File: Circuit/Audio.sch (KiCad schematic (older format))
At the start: 0 parts

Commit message: NAU8814 schematic component. LXDC2XQ footprint update. Kludge for forward/back slash in lib table needs addressing.
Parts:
- added U?: NAU8814, symbol NAU8814
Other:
- note added: "Mic Output - TRS jack?"
- note added: "Unused Analogue - Float\nUnused Digital - GND"
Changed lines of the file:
@@
 LIBS:lxdc2xq
 LIBS:qdtech-3.2-tft
+LIBS:nau8814
 LIBS:IoTuz-cache
 EELAYER 25 0
@@
 $Descr A4 11693 8268
 encoding utf-8
-Sheet 1 7
+Sheet 5 7
 Title ""
 Date ""
@@
 Comment4 ""
 $EndDescr
+$Comp
+L NAU8814 U?
+U 1 1 58192F60
+P 5600 3750
+F 0 "U?" H 5000 4450 60  0000 C CNN
+F 1 "NAU8814" H 6150 3050 60  0000 C CNN
+F 2 "" H 5600 3750 60  0001 C CNN
+F 3 "" H 5600 3750 60  0001 C CNN
+	1    5600 3750
+	1    0    0    -1
+$EndComp
+Text Notes 6300 4300 0    60   ~ 0
+Unused Analogue - Float\nUnused Digital - GND
+Text Notes 4350 2850 0    60   ~ 0
+Mic Output - TRS jack?
 $EndSCHEMATC

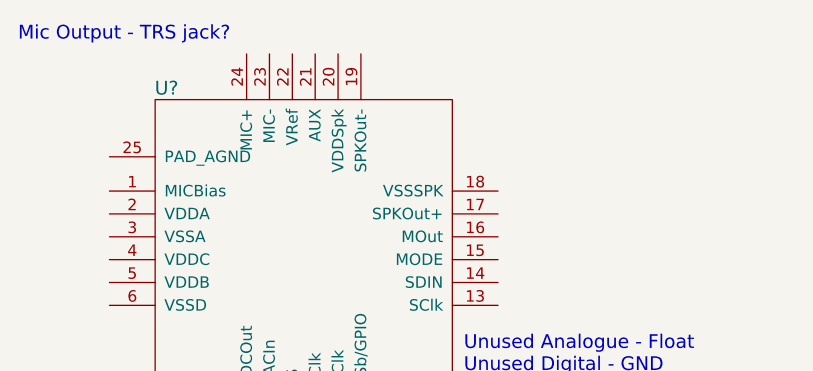
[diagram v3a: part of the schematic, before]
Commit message: Audio choices being narrowed.
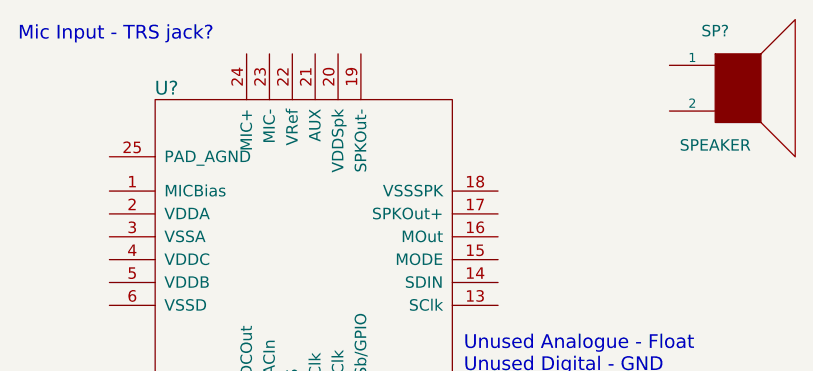
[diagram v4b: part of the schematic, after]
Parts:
- added SP?: SPEAKER, symbol SPEAKER
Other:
- note added: "Mic Input - TRS jack?"
- note removed: "Mic Output - TRS jack?"
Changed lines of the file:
@@
 Unused Analogue - Float\nUnused Digital - GND
 Text Notes 4350 2850 0    60   ~ 0
-Mic Output - TRS jack?
+Mic Input - TRS jack?
+$Comp
+L SPEAKER SP?
+U 1 1 581967C2
+P 7500 3050
+F 0 "SP?" H 7400 3300 50  0000 C CNN
+F 1 "SPEAKER" H 7400 2800 50  0000 C CNN
+F 2 "" H 7500 3050 50  0000 C CNN
+F 3 "" H 7500 3050 50  0000 C CNN
+F 4 "http://www.digikey.com.au/product-detail/en/cui-inc/CDM-12008/102-2494-ND/2791824" H 7500 3050 60  0001 C CNN "Link"
+F 5 "2.44000" H 7500 3050 60  0001 C CNN "Unit Cost"
+F 6 "102-2494-ND" H 7500 3050 60  0001 C CNN "Digikey PN"
+F 7 "CDM-12008" H 7500 3050 60  0001 C CNN "Manufacturer PN"
+	1    7500 3050
+	1    0    0    -1
+$EndComp
 $EndSCHEMATC

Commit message: Audio work, more to do.
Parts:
- added C?: 2.2uF, symbol C_Small
- added C? (x4): 4.7uF, symbol C
- added MK?: SPU0410HR5H, symbol SPU0410HR5H
- added R?: R, symbol R
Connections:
- net MICBias: now reaches U?.1 (MICBias)
- net MICBias: now also R?.1
- net AGND: now reaches U?.18 (VSSSPK)
- net AGND: now also U?.25 (PAD_AGND), U?.3 (VSSA), MK?.2 (GND), MK?.3 (GND)
- net +3V3: now reaches U?.20 (VDDSpk)
- net at U?.23 (MIC-): now also C?.2
- new net: MK?.1 (VIn), R?.2
- new net MICOut: C?.1, MK?.4 (Out)
- no-connect marks 0 -> 1
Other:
- note added: ""When the MIC- is used as a single ended input, \nMIC+ should be conned to VREF by setting PMICPGA[0] \naddress (0x2C) bit to LOW.""
- note added: "R needed?"
- note removed: "Mic Input - TRS jack?"
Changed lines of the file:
@@
 LIBS:qdtech-3.2-tft
 LIBS:nau8814
+LIBS:spu0410hr5h
 LIBS:IoTuz-cache
 EELAYER 25 0
@@
 Text Notes 6300 4300 0    60   ~ 0
 Unused Analogue - Float\nUnused Digital - GND
-Text Notes 4350 2850 0    60   ~ 0
-Mic Input - TRS jack?
 $Comp
 L SPEAKER SP?
@@
 	1    0    0    -1
 $EndComp
+Text Notes 600  900  0    60   ~ 0
+"When the MIC- is used as a single ended input, \nMIC+ should be conned to VREF by setting PMICPGA[0] \naddress (0x2C) bit to LOW."
+$Comp
+L SPU0410HR5H MK?
+U 1 1 581BC275
+P 1400 1900
+F 0 "MK?" H 1200 2200 60  0000 C CNN
+F 1 "SPU0410HR5H" H 900 1550 60  0000 C CNN
+F 2 "" H 1400 1900 60  0001 C CNN
+F 3 "" H 1400 1900 60  0001 C CNN
+	1    1400 1900
+	1    0    0    -1
+$EndComp
+NoConn ~ 5350 2900
+$Comp
+L C_Small C?
+U 1 1 581BC31F
+P 5450 2600
+F 0 "C?" H 5460 2670 50  0000 L CNN
+F 1 "2.2uF" H 5460 2520 50  0000 L CNN
+F 2 "" H 5450 2600 50  0000 C CNN
+F 3 "" H 5450 2600 50  0000 C CNN
+	1    5450 2600
+	1    0    0    -1
+$EndComp
+Text Label 4400 3500 0    60   ~ 0
+MICBias
+Wire Wire Line
+	4750 3500 4400 3500
+Text Label 1400 1150 0    60   ~ 0
+MICBias
+$Comp
+L R R?
+U 1 1 581BC437
+P 1400 1300
+F 0 "R?" V 1480 1300 50  0000 C CNN
+F 1 "R" V 1400 1300 50  0000 C CNN
+F 2 "" V 1330 1300 50  0000 C CNN
+F 3 "" H 1400 1300 50  0000 C CNN
+	1    1400 1300
+	1    0    0    -1
+$EndComp
+Wire Wire Line
+	5450 2200 5450 2500
+Wire Wire Line
+	5450 2700 5450 2900
+Text Label 4400 3350 0    60   ~ 0
+AGND
+Wire Wire Line
+	4400 3350 4750 3350
+Text Label 4400 3700 0    60   ~ 0
+AGND
+Wire Wire Line
+	4400 3700 4750 3700
+Text Label 1050 2550 0    60   ~ 0
+AGND
+Wire Wire Line
+	1050 2550 1400 2550
+Wire Wire Line
+	1300 2400 1300 2450
+Wire Wire Line
+	1300 2450 1500 2450
+Wire Wire Line
+	1400 2550 1400 2450
+Wire Wire Line
+	1500 2450 1500 2400
+Connection ~ 1400 2450
+$Comp
+L +3.3V #PWR?
+U 1 1 581BE27A
+P 5750 2750
+F 0 "#PWR?" H 5750 2600 50  0001 C CNN
+F 1 "+3.3V" H 5750 2890 50  0000 C CNN
+F 2 "" H 5750 2750 50  0000 C CNN
+F 3 "" H 5750 2750 50  0000 C CNN
+	1    5750 2750
+	1    0    0    -1
+$EndComp
+Wire Wire Line
+	5750 2750 5750 2900
+Text Label 5450 2200 0    60   ~ 0
+MICOut
+Text Label 1800 1900 0    60   ~ 0
+MICOut
+Text Notes 1550 1300 0    60   ~ 0
+R needed?
+Text Label 6600 3500 0    60   ~ 0
+AGND
+Wire Wire Line
+	6450 3500 6600 3500
+$Comp
+L C C?
+U 1 1 581BE775
+P 7850 3950
+F 0 "C?" H 7875 4050 50  0000 L CNN
+F 1 "4.7uF" H 7875 3850 50  0000 L CNN
+F 2 "" H 7888 3800 50  0000 C CNN
+F 3 "" H 7850 3950 50  0000 C CNN
+	1    7850 3950
+	1    0    0    -1
+$EndComp
+$Comp
+L C C?
+U 1 1 581BE7BE
+P 8100 3950
+F 0 "C?" H 8125 4050 50  0000 L CNN
+F 1 "4.7uF" H 8125 3850 50  0000 L CNN
+F 2 "" H 8138 3800 50  0000 C CNN
+F 3 "" H 8100 3950 50  0000 C CNN
+	1    8100 3950
+	1    0    0    -1
+$EndComp
+$Comp
+L C C?
+U 1 1 581BE7EF
+P 8350 3950
+F 0 "C?" H 8375 4050 50  0000 L CNN
+F 1 "4.7uF" H 8375 3850 50  0000 L CNN
+F 2 "" H 8388 3800 50  0000 C CNN
+F 3 "" H 8350 3950 50  0000 C CNN
+	1    8350 3950
+	1    0    0    -1
+$EndComp
+$Comp
+L C C?
+U 1 1 581BE825
+P 8600 3950
+F 0 "C?" H 8625 4050 50  0000 L CNN
+F 1 "4.7uF" H 8625 3850 50  0000 L CNN
+F 2 "" H 8638 3800 50  0000 C CNN
+F 3 "" H 8600 3950 50  0000 C CNN
+	1    8600 3950
+	1    0    0    -1
+$EndComp

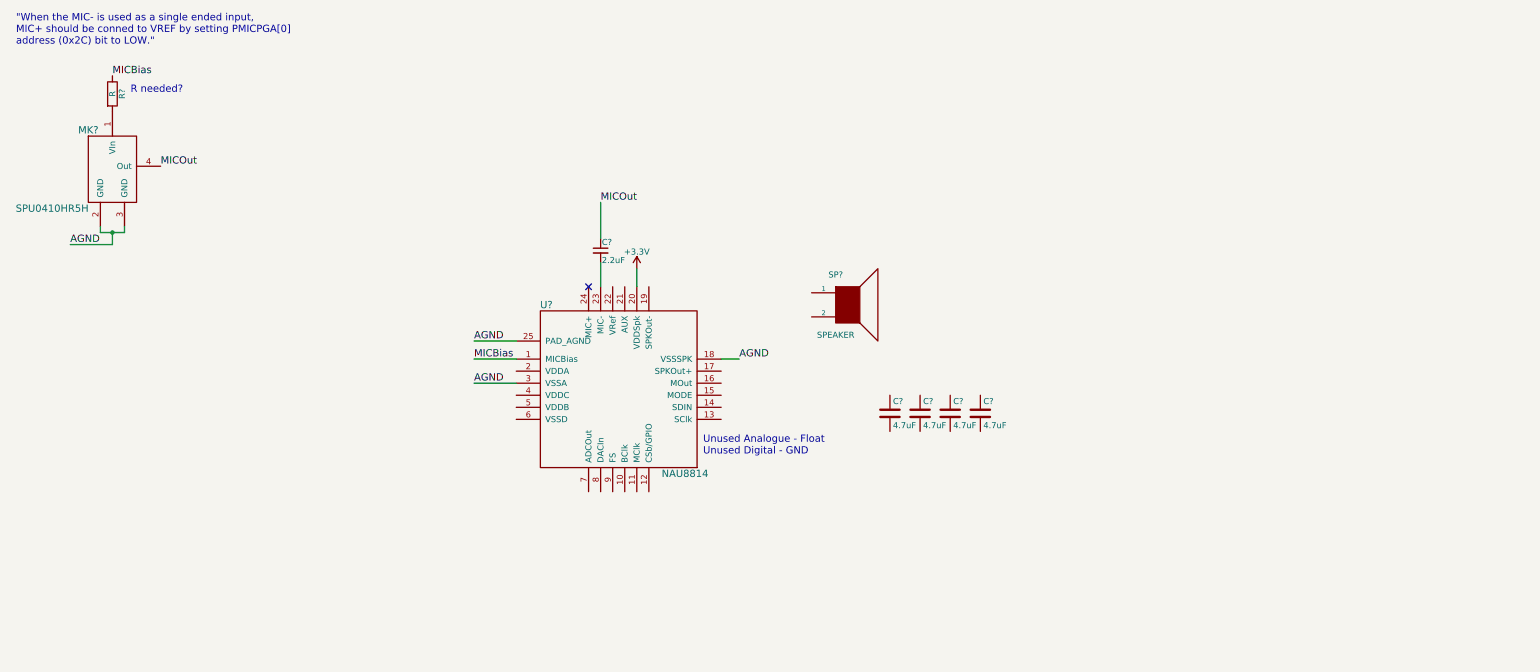
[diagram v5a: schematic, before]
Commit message: Audio updates & markup. Choices to be made, but can be completed just by adding i2s, i2c, & MCLK I/O.
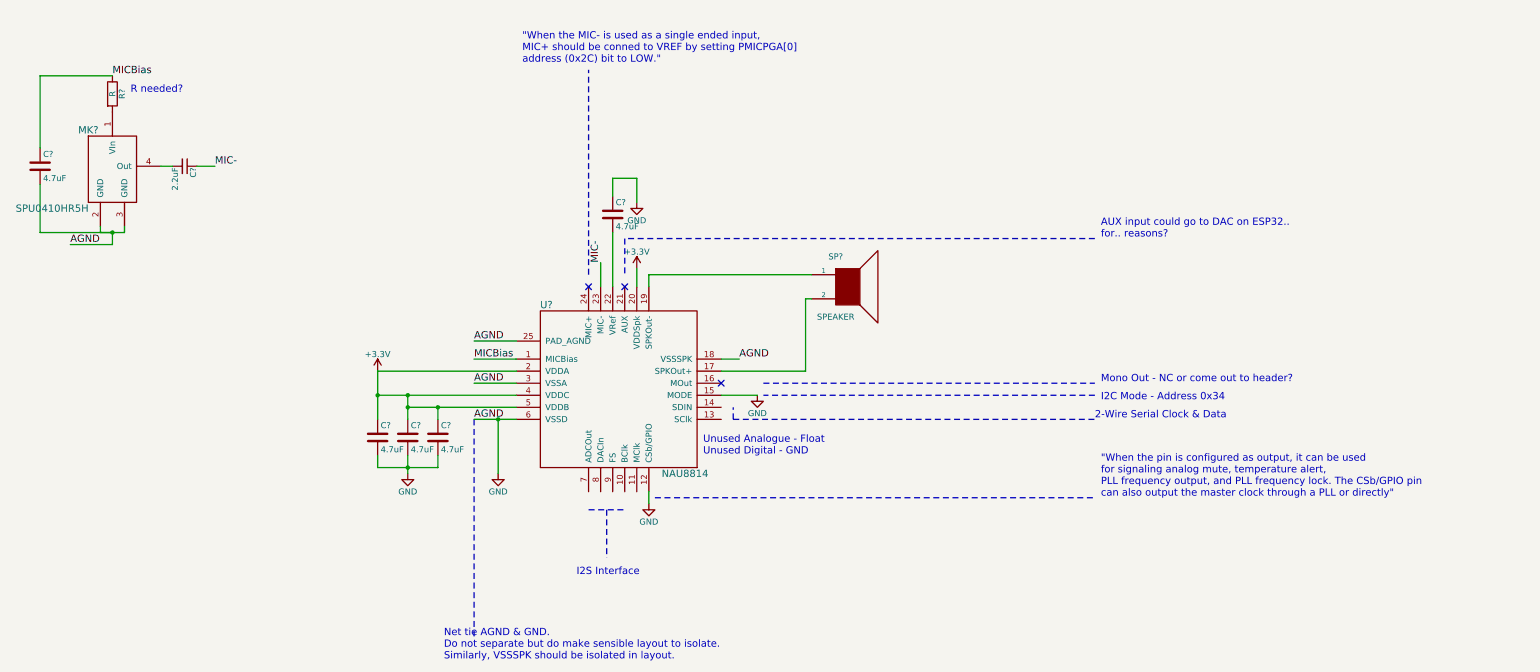
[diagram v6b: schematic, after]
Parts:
- added C?: 4.7uF, symbol C
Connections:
- net AGND is gone; now on net GND: MK?.2 (GND), MK?.3 (GND), U?.18 (VSSSPK), U?.25 (PAD_AGND), U?.3 (VSSA)
- net +3V3: now also C?.1, C?.1, C?.1, U?.2 (VDDA), U?.4 (VDDC), U?.5 (VDDB)
- net MICBias: now also C?.1
- net GND: now reaches U?.12 (CSb/GPIO)
- net GND: now also C?.1, C?.2, C?.2, C?.2, U?.15 (MODE), U?.6 (VSSD), C?.2
- net at U?.17 (SPKOut+): now also SP?.2
- net at U?.19 (SPKOut-): now also SP?.1
- net at U?.22 (VRef): now also C?.2
- net at C?.2: now also MK?.4 (Out); no longer U?.23 (MIC-)
- net MICOut renamed MIC-
- net MIC-: now also U?.23 (MIC-); no longer MK?.4 (Out)
- no-connect marks 1 -> 3
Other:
- note added: ""When the pin is configured as output, it can be used\nfor signaling analog mute, temperature alert, \nPLL frequency output, and PLL frequency lock. The CSb/GPIO pin\ncan also output the master clock through a PLL or directly""
- note added: "2-Wire Serial Clock & Data"
- note added: "AUX input could go to DAC on ESP32..\nfor.. reasons?"
- note added: "I2C Mode - Address 0x34"
- note added: "I2S Interface"
- note added: "Mono Out - NC or come out to header?"
- note added: "Net tie AGND & GND. \nDo not separate but do make sensible layout to isolate.\nSimilarly, VSSSPK should be isolated in layout."
- moved on the sheet: C?, SP?

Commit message: Audio hierarchical pins.
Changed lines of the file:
@@
 Text Notes 5250 5300 0    60   ~ 0
 I2S Interface
+Text HLabel 1400 3200 0    60   Input ~ 0
+MCLK
+Text HLabel 1400 3350 0    60   Input ~ 0
+SCLK
+Text HLabel 1400 3450 0    60   BiDi ~ 0
+SDIO
+Text HLabel 1400 3600 0    60   Input ~ 0
+FS
+Text HLabel 1400 3700 0    60   Input ~ 0
+BCLK
+Text HLabel 1400 3800 0    60   Input ~ 0
+DACIN
+Text HLabel 1400 3900 0    60   Output ~ 0
+ADCOUT
 $EndSCHEMATC

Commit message: Added Alligator clip points.
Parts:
- gave numbers to parts that had none: 10
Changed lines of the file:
@@
 $EndDescr
 $Comp
-L NAU8814 U?
+L NAU8814 U5
 U 1 1 58192F60
 P 5600 3750
-F 0 "U?" H 5000 4450 60  0000 C CNN
+F 0 "U5" H 5000 4450 60  0000 C CNN
 F 1 "NAU8814" H 6150 3050 60  0000 C CNN
 F 2 "" H 5600 3750 60  0001 C CNN
@@
 Unused Analogue - Float\nUnused Digital - GND
 $Comp
-L SPEAKER SP?
+L SPEAKER SP1
 U 1 1 581967C2
 P 7500 2900
-F 0 "SP?" H 7400 3150 50  0000 C CNN
+F 0 "SP1" H 7400 3150 50  0000 C CNN
 F 1 "SPEAKER" H 7400 2650 50  0000 C CNN
-F 2 "" H 7500 2900 50  0000 C CNN
+F 2 "" H 7500 2900 50  0001 C CNN
 F 3 "" H 7500 2900 50  0000 C CNN
 F 4 "http://www.digikey.com.au/product-detail/en/cui-inc/CDM-12008/102-2494-ND/2791824" H 7500 2900 60  0001 C CNN "Link"
@@
 "When the MIC- is used as a single ended input, \nMIC+ should be conned to VREF by setting PMICPGA[0] \naddress (0x2C) bit to LOW."
 $Comp
-L SPU0410HR5H MK?
+L SPU0410HR5H MK1
 U 1 1 581BC275
 P 1400 1900
-F 0 "MK?" H 1200 2200 60  0000 C CNN
+F 0 "MK1" H 1200 2200 60  0000 C CNN
 F 1 "SPU0410HR5H" H 900 1550 60  0000 C CNN
 F 2 "" H 1400 1900 60  0001 C CNN
@@
 NoConn ~ 5350 2900
 $Comp
-L C_Small C?
+L C_Small C2
 U 1 1 581BC31F
 P 2000 1900
-F 0 "C?" H 2010 1970 50  0000 L CNN
+F 0 "C2" H 2010 1970 50  0000 L CNN
 F 1 "2.2uF" H 2010 1820 50  0000 L CNN
-F 2 "" H 2000 1900 50  0000 C CNN
+F 2 "" H 2000 1900 50  0001 C CNN
 F 3 "" H 2000 1900 50  0000 C CNN
 	1    2000 1900
@@
 MICBias
 $Comp
-L R R?
+L R R15
 U 1 1 581BC437
 P 1400 1300
-F 0 "R?" V 1480 1300 50  0000 C CNN
+F 0 "R15" V 1480 1300 50  0000 C CNN
 F 1 "R" V 1400 1300 50  0000 C CNN
-F 2 "" V 1330 1300 50  0000 C CNN
+F 2 "" V 1330 1300 50  0001 C CNN
 F 3 "" H 1400 1300 50  0000 C CNN
 	1    1400 1300
@@
 Connection ~ 1400 2450
 $Comp
-L +3.3V #PWR?
+L +3.3V #PWR060
 U 1 1 581BE27A
 P 5750 2750
-F 0 "#PWR?" H 5750 2600 50  0001 C CNN
+F 0 "#PWR060" H 5750 2600 50  0001 C CNN
 F 1 "+3.3V" H 5750 2890 50  0000 C CNN
 F 2 "" H 5750 2750 50  0000 C CNN
@@
 	6450 3500 6600 3500
 $Comp
-L C C?
+L C C16
 U 1 1 581BE775
 P 5550 2300
-F 0 "C?" H 5575 2400 50  0000 L CNN
+F 0 "C16" H 5575 2400 50  0000 L CNN
 F 1 "4.7uF" H 5575 2200 50  0000 L CNN
-F 2 "" H 5588 2150 50  0000 C CNN
+F 2 "" H 5588 2150 50  0001 C CNN
 F 3 "" H 5550 2300 50  0000 C CNN
 	1    5550 2300
@@
 $EndComp
 $Comp
-L C C?
+L C C13
 U 1 1 581BE7BE
 P 3600 4150
-F 0 "C?" H 3625 4250 50  0000 L CNN
+F 0 "C13" H 3625 4250 50  0000 L CNN
 F 1 "4.7uF" H 3625 4050 50  0000 L CNN
-F 2 "" H 3638 4000 50  0000 C CNN
+F 2 "" H 3638 4000 50  0001 C CNN
 F 3 "" H 3600 4150 50  0000 C CNN
 	1    3600 4150
@@
 $EndComp
 $Comp
-L C C?
+L C C14
 U 1 1 581BE7EF
 P 3850 4150
-F 0 "C?" H 3875 4250 50  0000 L CNN
+F 0 "C14" H 3875 4250 50  0000 L CNN
 F 1 "4.7uF" H 3875 4050 50  0000 L CNN
-F 2 "" H 3888 4000 50  0000 C CNN
+F 2 "" H 3888 4000 50  0001 C CNN
 F 3 "" H 3850 4150 50  0000 C CNN
 	1    3850 4150
@@
 $EndComp
 $Comp
-L C C?
+L C C15
 U 1 1 581BE825
 P 4100 4150
-F 0 "C?" H 4125 4250 50  0000 L CNN
+F 0 "C15" H 4125 4250 50  0000 L CNN
 F 1 "4.7uF" H 4125 4050 50  0000 L CNN
-F 2 "" H 4138 4000 50  0000 C CNN
+F 2 "" H 4138 4000 50  0001 C CNN
 F 3 "" H 4100 4150 50  0000 C CNN
 	1    4100 4150
@@
 	2100 1900 2250 1900
 $Comp
-L GND #PWR?
+L GND #PWR061
 U 1 1 581BEFAA
 P 5750 2200
-F 0 "#PWR?" H 5750 1950 50  0001 C CNN
+F 0 "#PWR061" H 5750 1950 50  0001 C CNN
 F 1 "GND" H 5750 2050 50  0000 C CNN
 F 2 "" H 5750 2200 50  0000 C CNN
@@
 	5550 2450 5550 2900
 $Comp
-L C C?
+L C C1
 U 1 1 581BF169
 P 800 1900
-F 0 "C?" H 825 2000 50  0000 L CNN
+F 0 "C1" H 825 2000 50  0000 L CNN
 F 1 "4.7uF" H 825 1800 50  0000 L CNN
-F 2 "" H 838 1750 50  0000 C CNN
+F 2 "" H 838 1750 50  0001 C CNN
 F 3 "" H 800 1900 50  0000 C CNN
 	1    800  1900
@@
 	800  2450 800  2050
 $Comp
-L GND #PWR?
+L GND #PWR062
 U 1 1 581BF41C
 P 6750 3800
-F 0 "#PWR?" H 6750 3550 50  0001 C CNN
+F 0 "#PWR062" H 6750 3550 50  0001 C CNN
 F 1 "GND" H 6750 3650 50  0000 C CNN
 F 2 "" H 6750 3800 50  0000 C CNN
@@
 Mono Out - NC or come out to header?
 $Comp
-L GND #PWR?
+L GND #PWR063
 U 1 1 581BFD59
 P 4600 4450
-F 0 "#PWR?" H 4600 4200 50  0001 C CNN
+F 0 "#PWR063" H 4600 4200 50  0001 C CNN
 F 1 "GND" H 4600 4300 50  0000 C CNN
 F 2 "" H 4600 4450 50  0000 C CNN
@@
 Connection ~ 3850 3800
 $Comp
-L +3.3V #PWR?
+L +3.3V #PWR064
 U 1 1 581C0164
 P 3600 3600
-F 0 "#PWR?" H 3600 3450 50  0001 C CNN
+F 0 "#PWR064" H 3600 3450 50  0001 C CNN
 F 1 "+3.3V" H 3600 3740 50  0000 C CNN
 F 2 "" H 3600 3600 50  0000 C CNN
@@
 $EndComp
 $Comp
-L GND #PWR?
+L GND #PWR065
 U 1 1 581C01A1
 P 3850 4450
-F 0 "#PWR?" H 3850 4200 50  0001 C CNN
+F 0 "#PWR065" H 3850 4200 50  0001 C CNN
 F 1 "GND" H 3850 4300 50  0000 C CNN
 F 2 "" H 3850 4450 50  0000 C CNN
@@
 AUX input could go to DAC on ESP32..\nfor.. reasons?
 $Comp
-L GND #PWR?
+L GND #PWR066
 U 1 1 581C0598
 P 5850 4700
-F 0 "#PWR?" H 5850 4450 50  0001 C CNN
+F 0 "#PWR066" H 5850 4450 50  0001 C CNN
 F 1 "GND" H 5850 4550 50  0000 C CNN
 F 2 "" H 5850 4700 50  0000 C CNN
